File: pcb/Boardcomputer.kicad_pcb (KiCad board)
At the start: 2 copper layers, 17 parts, among them J1 Receiver, J2 5V Input, J3 5V Reg VCC, M1 Winch Rear, M2 Motor, M3 Winch Front, M4 Steering Servo, Q1 Motor VCC, U1 ESP32 C3 SUPERMINI, U2 Winch Rear VCC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

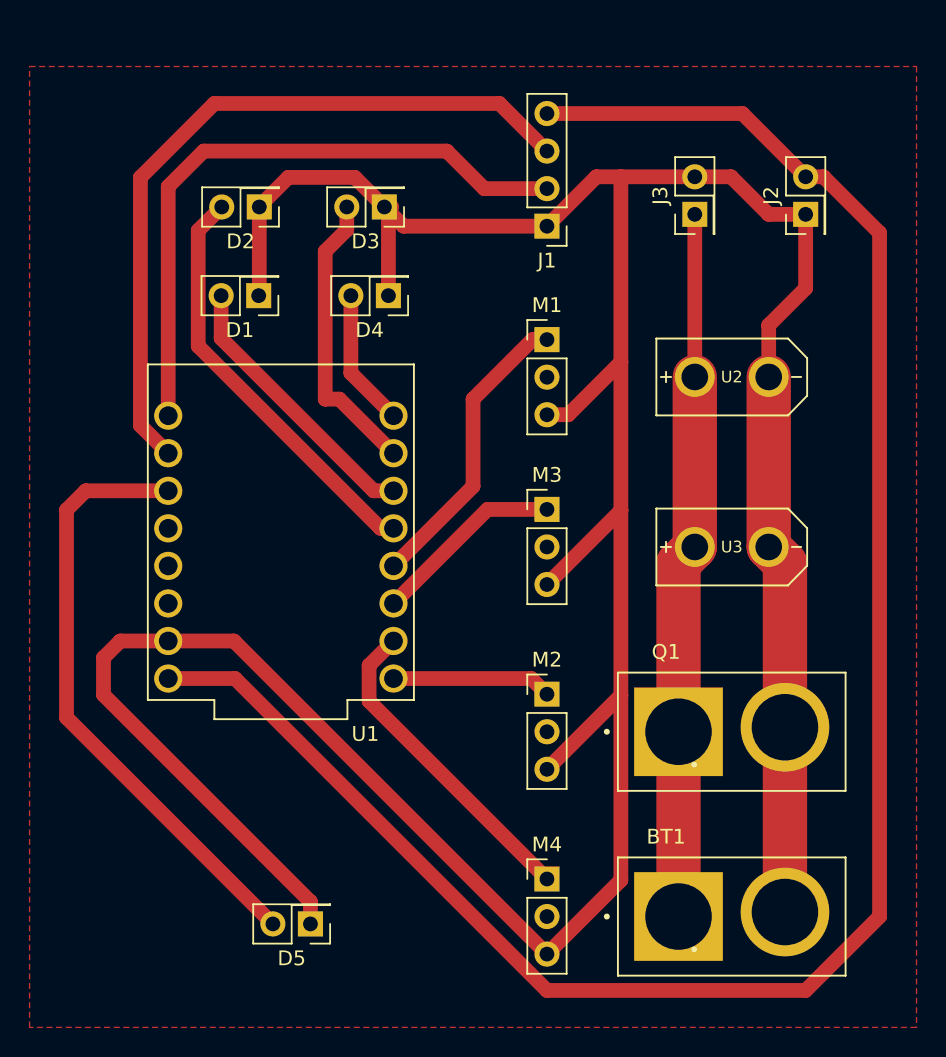
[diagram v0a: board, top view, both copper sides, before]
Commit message: Way too much stuff for one commit... essentially made everything configurable through a web ui
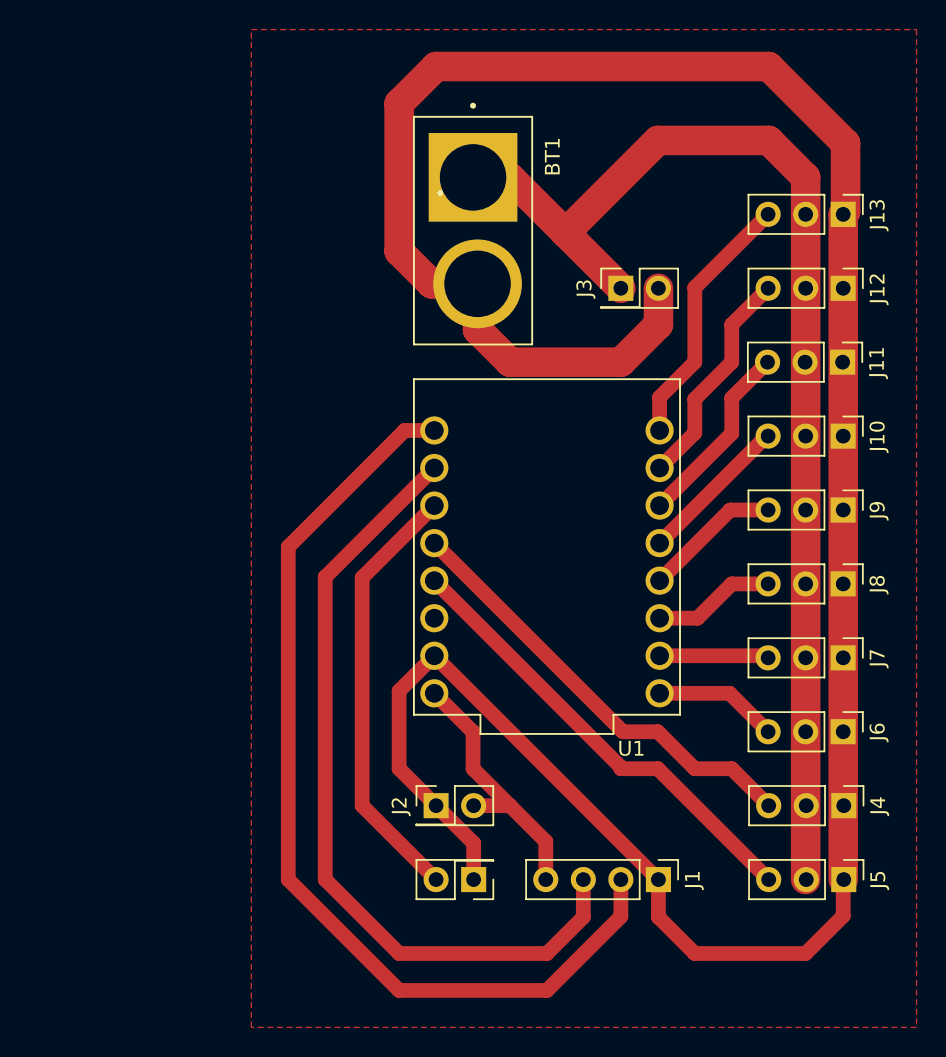
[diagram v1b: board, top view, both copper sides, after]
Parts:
- removed D1: Blinker Left, Connector_PinHeader_2.54mm:PinHeader_2x01_P2.54mm_Vertical
- removed D2: Headlight, Connector_PinHeader_2.54mm:PinHeader_2x01_P2.54mm_Vertical
- removed D3: Blinker Right, Connector_PinHeader_2.54mm:PinHeader_2x01_P2.54mm_Vertical
- removed D4: Breaklight, Connector_PinHeader_2.54mm:PinHeader_2x01_P2.54mm_Vertical
- removed M1: Winch Rear, Connector_PinHeader_2.54mm:PinHeader_1x03_P2.54mm_Vertical
- removed M2: Motor, Connector_PinHeader_2.54mm:PinHeader_1x03_P2.54mm_Vertical
- removed M3: Winch Front, Connector_PinHeader_2.54mm:PinHeader_1x03_P2.54mm_Vertical
- removed M4: Steering Servo, Connector_PinHeader_2.54mm:PinHeader_1x03_P2.54mm_Vertical
- removed Q1: Motor VCC, Library:AMASS_XT60PB-M
- removed U2: Winch Rear VCC, Library:XT30UPB-M
- removed U3: Winch Front VCC, Library:XT30UPB-M
- added J10: AUX5, Connector_PinHeader_2.54mm:PinHeader_1x03_P2.54mm_Vertical, F.Cu at (152.5, 70.0)
- added J11: AUX6, Connector_PinHeader_2.54mm:PinHeader_1x03_P2.54mm_Vertical, F.Cu at (152.5, 65.0)
- added J12: AUX7, Connector_PinHeader_2.54mm:PinHeader_1x03_P2.54mm_Vertical, F.Cu at (152.5, 60.0)
- added J13: AUX8, Connector_PinHeader_2.54mm:PinHeader_1x03_P2.54mm_Vertical, F.Cu at (152.5, 55.0)
- added J4: Motor, Connector_PinHeader_2.54mm:PinHeader_1x03_P2.54mm_Vertical, F.Cu at (152.6, 95.0)
- added J5: Steering, Connector_PinHeader_2.54mm:PinHeader_1x03_P2.54mm_Vertical, F.Cu at (152.6, 100.0)
- added J6: AUX1, Connector_PinHeader_2.54mm:PinHeader_1x03_P2.54mm_Vertical, F.Cu at (152.5, 90.0)
- added J7: AUX2, Connector_PinHeader_2.54mm:PinHeader_1x03_P2.54mm_Vertical, F.Cu at (152.5, 85.0)
- added J8: AUX3, Connector_PinHeader_2.54mm:PinHeader_1x03_P2.54mm_Vertical, F.Cu at (152.5, 80.0)
- added J9: AUX4, Connector_PinHeader_2.54mm:PinHeader_1x03_P2.54mm_Vertical, F.Cu at (152.5, 75.0)
- moved BT1 49.6 mm to (127.5, 56.1), turned to -90 degrees
- moved J2 47.2 mm to (125.0, 95.0), turned to 0 degrees
- moved J1 44.8 mm to (140.0, 100.0), turned to -90 degrees
- moved U1 18.0 mm to (132.5, 77.5)
- moved D5 11.4 mm to (127.5, 100.0)
- moved J3 7.07 mm to (137.5, 60.0), turned to 0 degrees
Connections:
- U1 pad 3: unconnected-(U1-GPIO3-Pad3) -> Net-(J4-Pin_3)
- U1 pad 4: unconnected-(U1-GPIO4-Pad4) -> Net-(J5-Pin_3)
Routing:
- net +5V: track 130.5 -> 18.2 mm
- net +BATT: track 48.0 -> 128.0 mm
- net GND: track 241.3 -> 178.5 mm
- net Net-(J5-Pin_3): track 0.00 -> 31.1 mm
- net Net-(J4-Pin_3): track 0.00 -> 30.0 mm
- net Net-(J1-Pin_2): track 43.2 -> 65.8 mm
- net Net-(J10-Pin_3): track 28.4 -> 10.3 mm
- net Net-(J7-Pin_3): track 21.8 -> 7.40 mm
- net Net-(D5-A): track 41.2 -> 29.4 mm
- net Net-(J9-Pin_3): track 20.2 -> 9.32 mm
- net Net-(J13-Pin_3): track 9.32 -> 17.7 mm
- net Net-(J11-Pin_3): track 18.8 -> 12.7 mm
- net Net-(J8-Pin_3): track 13.0 -> 8.30 mm
- net Net-(J12-Pin_3): track 19.7 -> 15.2 mm
- net Net-(J1-Pin_3): track 50.3 -> 54.0 mm
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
